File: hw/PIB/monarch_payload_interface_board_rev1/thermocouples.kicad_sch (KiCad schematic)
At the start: 6 parts, among them U3 MAX31856MUD_T

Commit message: Schematic Review
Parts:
- added C26, C28, C29, C31, C33, C34, C36, C38, C39, C41, C43, C44: 0.01u, Capacitor_SMD:C_0603_1608Metric, symbol Device:C_Small
- added C27, C30, C32, C35, C37, C40, C42, C45: 0.1u, Capacitor_SMD:C_0603_1608Metric, symbol Device:C_Small
- added U5, U6, U7, U8: MAX31856MUD_T, MAX31856MUD_T:SOP65P640X110-14N, symbol MAX31856MUD_T:MAX31856MUD_T
- C21, C22, C23, C24, C25: footprint (none) -> Capacitor_SMD:C_0603_1608Metric
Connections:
- net +3V3: now also C29.2, C30.1, C34.2, C35.1, C39.2, C40.1, C44.2, C45.1, U5.5 (AVDD), U5.8 (DVDD), U6.5 (AVDD), U6.8 (DVDD), U7.5 (AVDD), U7.8 (DVDD), U8.5 (AVDD), U8.8 (DVDD)
- net GND: now also C26.1, C28.2, C29.1, C30.2, C31.1, C33.2, C34.1, C35.2, C36.1, C38.2, C39.1, C40.2, C41.1, C43.2, C44.1, C45.2, U5.1 (AGND), U5.14 (DGND), U6.1 (AGND), U6.14 (DGND), U7.1 (AGND), U7.14 (DGND), U8.1 (AGND), U8.14 (DGND)
- net SPI3_MISO: now also U5.11 (SDO), U6.11 (SDO), U7.11 (SDO), U8.11 (SDO)
- net SPI3_MOSI: now also U5.12 (SDI), U6.12 (SDI), U7.12 (SDI), U8.12 (SDI)
- net SPI3_SCK: now also U5.10 (SCK), U6.10 (SCK), U7.10 (SCK), U8.10 (SCK)
- net T1+: now also C26.2, C27.1, U5.4 (T+); no longer C21.2, C23.1, U3.4 (T+)
- net T1-: now also C27.2, C28.1, U5.2 (BIAS), U5.3 (T-); no longer C22.1, C23.2, U3.2 (BIAS), U3.3 (T-)
- net T1: now reaches U3.9 (~{CS})
- new net T0+: C21.2, C23.1, U3.4 (T+)
- new net T0-: C22.1, C23.2, U3.2 (BIAS), U3.3 (T-)
- new net T2: U5.9 (~{CS})
- new net T2+: C31.2, C32.1, U6.4 (T+)
- new net T2-: C32.2, C33.1, U6.2 (BIAS), U6.3 (T-)
- new net T3: U6.9 (~{CS})
- new net T3+: C36.2, C37.1, U7.4 (T+)
- new net T3-: C37.2, C38.1, U7.2 (BIAS), U7.3 (T-)
- new net T4: U7.9 (~{CS})
- new net T4+: C41.2, C42.1, U8.4 (T+)
- new net T4-: C42.2, C43.1, U8.2 (BIAS), U8.3 (T-)
- new net T5: U8.9 (~{CS})
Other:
- moved on the sheet: C21, C22, C23, C24, C25, U3

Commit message: PIB Layout Update 3/2
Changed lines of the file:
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@@
 	)
 	(junction
-		(at 219.71 59.69)
-		(diameter 0)
-		(color 0 0 0 0)
-	)
-	(junction
 		(at 177.8 109.22)
 		(diameter 0)
@@
 	(wire
 		(pts
-			(xy 219.71 59.69) (xy 219.71 62.23)
-		)
-		(stroke
-			(width 0)
-			(type default)
-		)
-	)
-	(wire
-		(pts
 			(xy 59.69 72.39) (xy 66.04 72.39)
 		)
@@
 	(wire
 		(pts
-			(xy 219.71 59.69) (xy 220.98 59.69)
-		)
-		(stroke
-			(width 0)
-			(type default)
-		)
-	)
-	(wire
-		(pts
 			(xy 212.09 114.3) (xy 212.09 115.57)
 		)
@@
 	(wire
 		(pts
-			(xy 215.9 59.69) (xy 219.71 59.69)
+			(xy 215.9 59.69) (xy 220.98 59.69)
 		)
 		(stroke
@@
 					(unit 1)
 				)
+			)
+		)
+	)
+	(symbol
+		(lib_id "power:+3V3")
+		(at 219.71 62.23 270)
+		(unit 1)
+		(exclude_from_sim no)
+		(in_bom yes)
+		(on_board yes)
+		(dnp no)
+		(fields_autoplaced yes)
+		(property "Reference" "#PWR0218"
+			(at 215.9 62.23 0)
+			(effects
+				(font
+					(size 1.27 1.27)
+				)
+				(hide yes)
+			)
+		)
+		(property "Value" "+3V3"
+			(at 223.52 62.2299 90)
+			(effects
+				(font
+					(size 1.27 1.27)
+				)
+				(justify left)
+			)
+		)
+		(property "Footprint" ""
+			(at 219.71 62.23 0)
+			(effects
+				(font
+					(size 1.27 1.27)
+				)
+				(hide yes)
+			)
+		)
+		(property "Datasheet" ""
+			(at 219.71 62.23 0)
+			(effects
+				(font
+					(size 1.27 1.27)
+				)
+				(hide yes)
+			)
+		)
+		(property "Description" "Power symbol creates a global label with name \"+3V3\""
+			(at 219.71 62.23 0)
+			(effects
+				(font
+					(size 1.27 1.27)
+				)
+				(hide yes)
+			)
+		)
+		(pin "1"
+		)
+		(instances
+			(project "monarch_payload_interface_board_rev1"
+				(path "/bf7ee58d-ac53-49d1-a6b2-96a87d67b737/4eb43b0e-6885-46a5-9a94-7deafa1b26d8"
+					(reference "#PWR0218")
+					(unit 1)
+				)

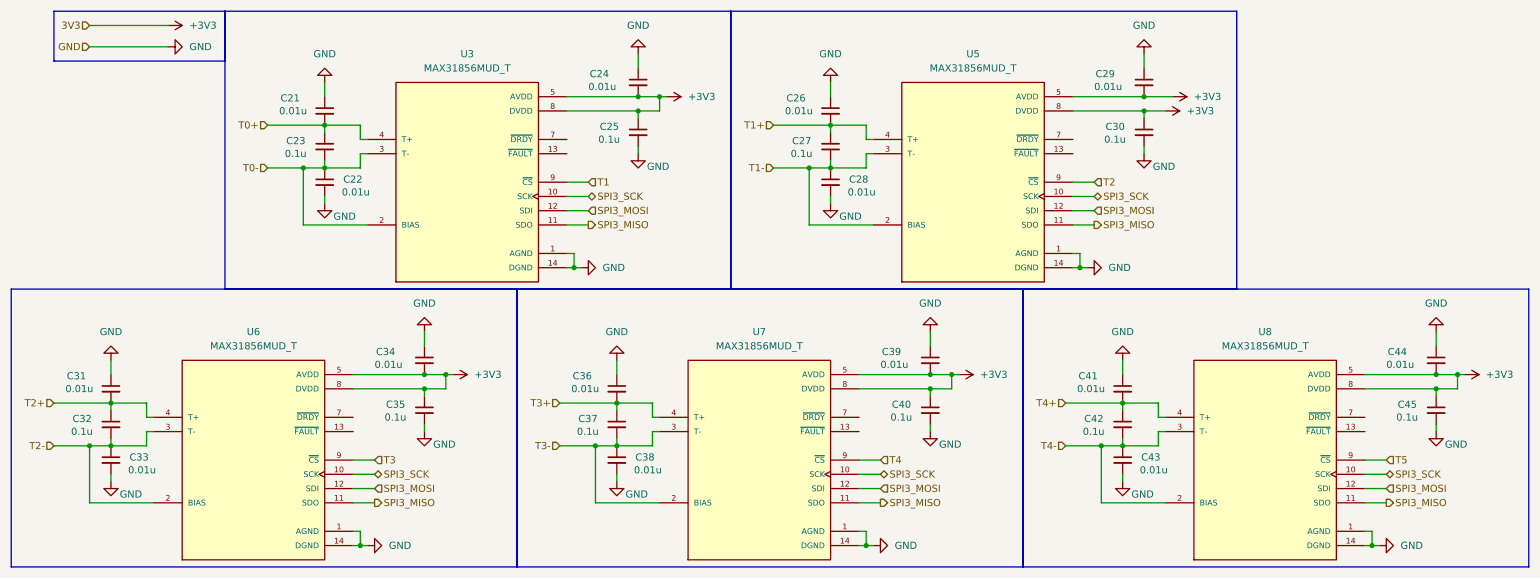
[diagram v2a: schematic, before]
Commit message: PIB layout update
done pending Ben O approval
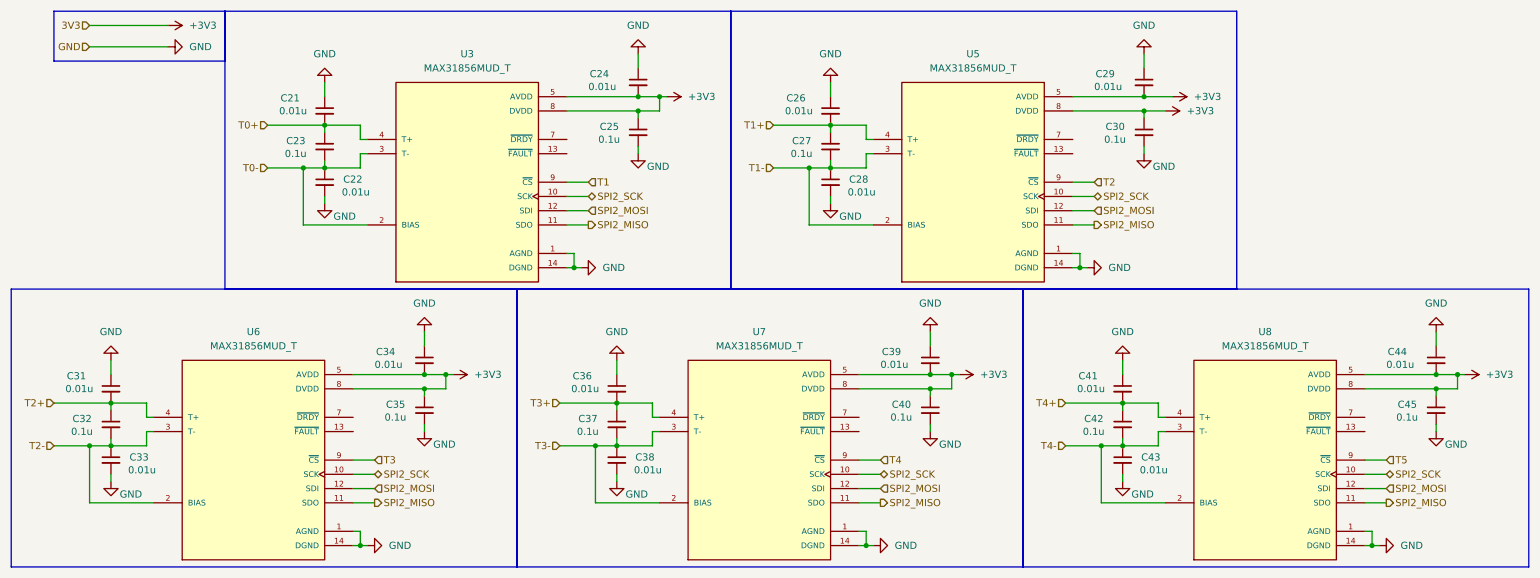
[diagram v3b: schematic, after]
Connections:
- net SPI3_MISO renamed SPI2_MISO
- net SPI3_MOSI renamed SPI2_MOSI
- net SPI3_SCK renamed SPI2_SCK
